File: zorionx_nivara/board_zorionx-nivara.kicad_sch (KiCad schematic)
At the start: 3 parts, among them U1 ESP32-S3-WROOM-1

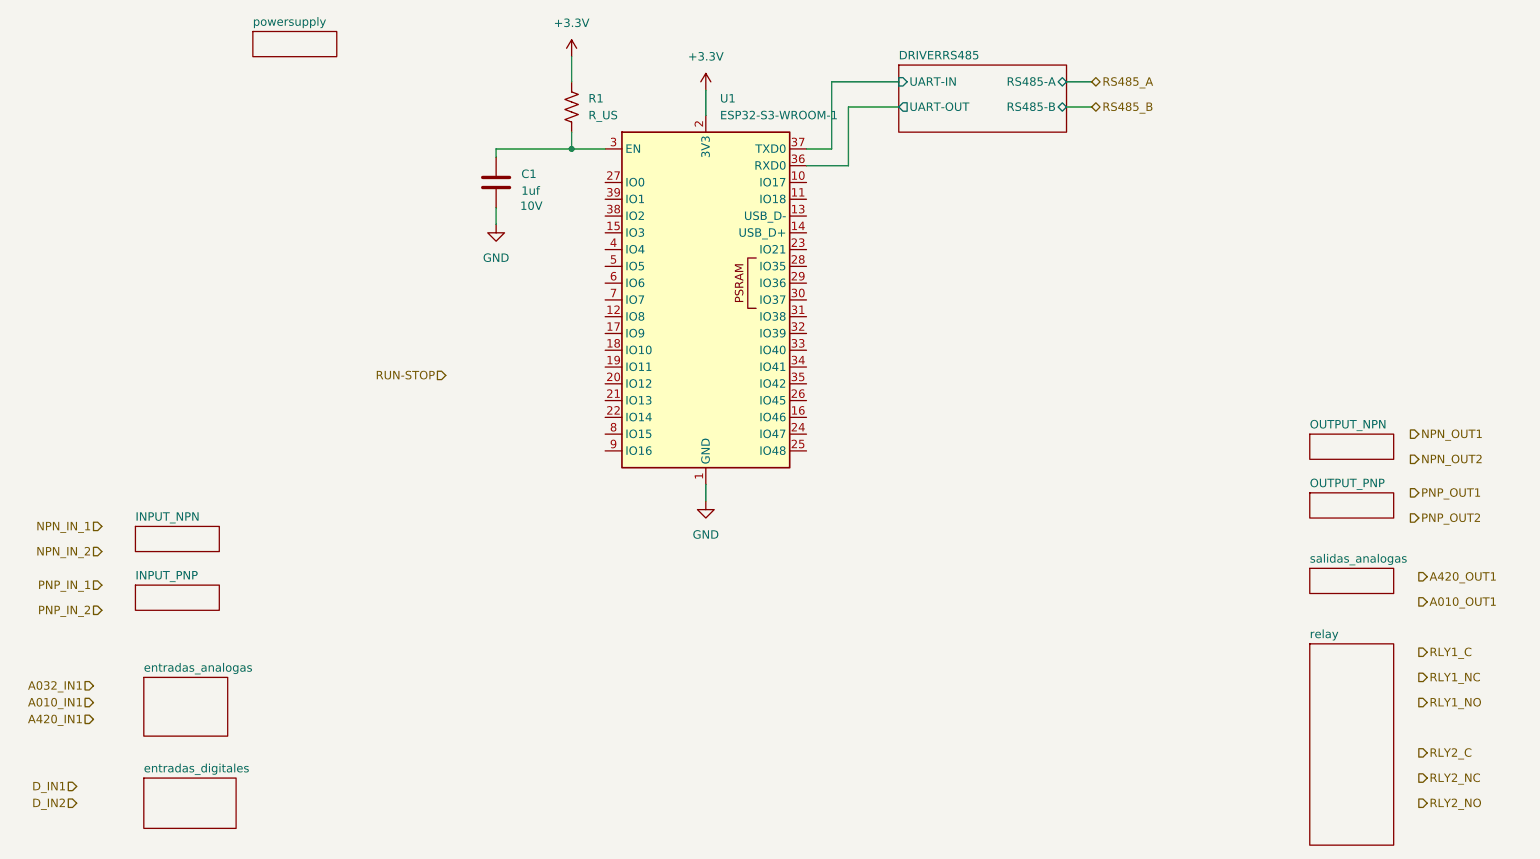
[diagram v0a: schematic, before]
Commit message: ruteo power
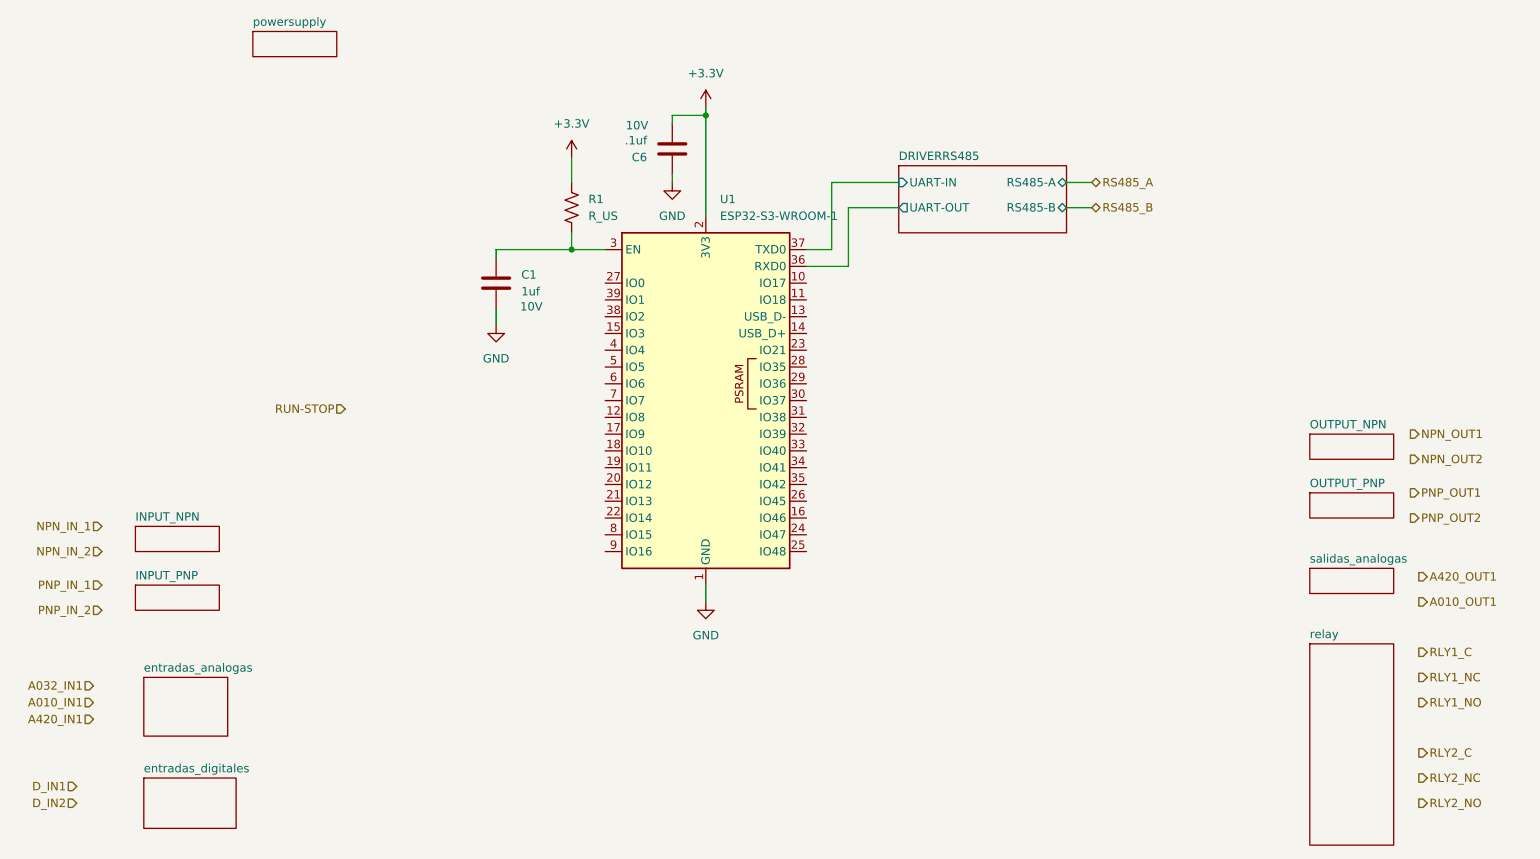
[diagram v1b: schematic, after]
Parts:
- added C6: .1uf, Capacitor_SMD:C_0201_0603Metric, symbol Device:C
- C1: footprint (none) -> Capacitor_SMD:C_0201_0603Metric
- R1: footprint (none) -> Resistor_SMD:R_0201_0603Metric
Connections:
- net +3.3V: now also C6.2
- net GND: now also C6.1
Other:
- moved on the sheet: C1, R1, U1

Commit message: driver relay
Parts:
- added D1: SM712_SOT23, Package_TO_SOT_SMD:SOT-23, symbol Diode:SM712_SOT23
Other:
- sheet relay ports: added RELAY_1_IN, RELAY_2_IN, RLY1_C, RLY1_NC, RLY1_NO, RLY2_C, RLY2_NC, RLY2_NO; removed none
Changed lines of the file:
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@@
+	(wire
+		(pts
+			(xy 242.57 129.54) (xy 248.92 129.54)
+		)
+		(stroke
+			(width 0)
+			(type default)
+		)
+	)
 	(wire
 		(pts
@@
 	(wire
 		(pts
+			(xy 242.57 114.3) (xy 248.92 114.3)
+		)
+		(stroke
+			(width 0)
+			(type default)
+		)
+	)
+	(wire
+		(pts
 			(xy 190.5 43.18) (xy 194.31 43.18)
 		)
@@
 	(wire
 		(pts
+			(xy 242.57 125.73) (xy 248.92 125.73)
+		)
+		(stroke
+			(width 0)
+			(type default)
+		)
+	)
+	(wire
+		(pts
+			(xy 242.57 133.35) (xy 248.92 133.35)
+		)
+		(stroke
+			(width 0)
+			(type default)
+		)
+	)
+	(wire
+		(pts
 			(xy 135.89 29.21) (xy 135.89 44.45)
 		)
@@
 	(wire
 		(pts
+			(xy 242.57 110.49) (xy 248.92 110.49)
+		)
+		(stroke
+			(width 0)
+			(type default)
+		)
+	)
+	(wire
+		(pts
 			(xy 115.57 46.99) (xy 115.57 49.53)
 		)
@@
 		(pts
 			(xy 130.81 38.1) (xy 130.81 39.37)
+		)
+		(stroke
+			(width 0)
+			(type default)
+		)
+	)
+	(wire
+		(pts
+			(xy 242.57 118.11) (xy 248.92 118.11)
 		)
 		(stroke
@@
 	(hierarchical_label "RLY2_NC"
 		(shape output)
-		(at 243.84 129.54 0)
+		(at 248.92 129.54 0)
 		(effects
 			(font
@@
 	(hierarchical_label "RLY2_C"
 		(shape output)
-		(at 243.84 125.73 0)
+		(at 248.92 125.73 0)
 		(effects
 			(font
@@
 	(hierarchical_label "RLY2_NO"
 		(shape output)
-		(at 243.84 133.35 0)
+		(at 248.92 133.35 0)
 		(effects
 			(font
@@
 	(hierarchical_label "RLY1_NC"
 		(shape output)
-		(at 243.84 114.3 0)
+		(at 248.92 114.3 0)
 		(effects
 			(font
@@
 	(hierarchical_label "RLY1_C"
 		(shape output)
-		(at 243.84 110.49 0)
+		(at 248.92 110.49 0)
 		(effects
 			(font
@@
 	(hierarchical_label "RLY1_NO"
 		(shape output)
-		(at 243.84 118.11 0)
+		(at 248.92 118.11 0)
 		(effects
 			(font
@@
 			)
 			(justify left)
+		)
+	)
+	(symbol
+		(lib_id "Diode:SM712_SOT23")
+		(at 181.61 86.36 0)
+		(unit 1)
+		(exclude_from_sim no)
+		(in_bom yes)
+		(on_board yes)
+		(dnp no)
+		(fields_autoplaced yes)
+		(property "Reference" "D1"
+			(at 181.61 80.01 0)
+			(effects
+				(font
+					(size 1.27 1.27)
+				)
+			)
+		)
+		(property "Value" "SM712_SOT23"
+			(at 181.61 82.55 0)
+			(effects
+				(font
+					(size 1.27 1.27)
+				)
+			)
+		)
+		(property "Footprint" "Package_TO_SOT_SMD:SOT-23"
+			(at 181.61 95.25 0)
+			(effects
+				(font
+					(size 1.27 1.27)
+				)
+				(hide yes)
+			)
+		)
+		(property "Datasheet" "https://www.littelfuse.com/~/media/electronics/datasheets/tvs_diode_arrays/littelfuse_tvs_diode_array_sm712_datasheet.pdf.pdf"
+			(at 177.8 86.36 0)
+			(effects
+				(font
+					(size 1.27 1.27)
+				)
+				(hide yes)
+			)
+		)
+		(property "Description" "7V/12V, 600W Asymmetrical TVS Diode Array, SOT-23"
+			(at 181.61 86.36 0)
+			(effects
+				(font
+					(size 1.27 1.27)
+				)
+				(hide yes)
+			)
+		)
+		(pin "2"
+		)
+		(pin "1"
+		)
+		(pin "3"
+		)
+		(instances
+			(project ""
+				(path "/f2de36b2-81cb-4123-9a7d-6a58bb468c83/5c2764ec-6d16-4e1c-b9c0-76c16778bf20"
+					(reference "D1")
+					(unit 1)
+				)
+			)
 		)
 	)
@@
 	)
 	(sheet
-		(at 227.33 109.22)
-		(size 12.7 30.48)
+		(at 215.9 107.95)
+		(size 26.67 27.94)
 		(exclude_from_sim no)
 		(in_bom yes)
@@
 		)
 		(property "Sheetname" "relay"
-			(at 227.33 108.5084 0)
+			(at 215.9 107.2384 0)
 			(effects
 				(font
@@
 		)
 		(property "Sheetfile" "relay.kicad_sch"
-			(at 227.33 140.2846 0)
+			(at 215.9 136.4746 0)
 			(effects
 				(font
@@
 			)
 		)
+		(pin "RELAY_1_IN" input
+			(at 215.9 113.03 180)
+			(effects
+				(font
+					(size 1.27 1.27)
+				)
+				(justify left)
+			)
+		)
+		(pin "RELAY_2_IN" input
+			(at 215.9 120.65 180)
+			(effects
+				(font
+					(size 1.27 1.27)
+				)
+				(justify left)
+			)
+		)
+		(pin "RLY1_C" output
+			(at 242.57 110.49 0)
+			(effects
+				(font
+					(size 1.27 1.27)
+				)
+				(justify right)
+			)
+		)
+		(pin "RLY1_NC" output
+			(at 242.57 114.3 0)
+			(effects
+				(font
+					(size 1.27 1.27)
+				)
+				(justify right)
+			)
+		)
+		(pin "RLY1_NO" output
+			(at 242.57 118.11 0)
+			(effects
+				(font
+					(size 1.27 1.27)
+				)
+				(justify right)
+			)
+		)
+		(pin "RLY2_C" output
+			(at 242.57 125.73 0)
+			(effects
+				(font
+					(size 1.27 1.27)
+				)
+				(justify right)
+			)
+		)
+		(pin "RLY2_NC" output
+			(at 242.57 129.54 0)
+			(effects
+				(font
+					(size 1.27 1.27)
+				)
+				(justify right)
+			)
+		)
+		(pin "RLY2_NO" output
+			(at 242.57 133.35 0)
+			(effects
+				(font
+					(size 1.27 1.27)
+				)
+				(justify right)
+			)
+		)
